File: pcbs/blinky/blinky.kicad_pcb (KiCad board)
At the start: 4 copper layers, 64 x 72 mm, 184 parts, among them J1 JACK IN, J2 NEOPIXEL, Q1 PMBT2222A,215, SW1 TACTILE, SW2 POWER, U1 ATSAMD21E17, U2 MIC5225-3.3YM5, U3 TSOP75438WTT, U4 IS31FL3731-SALS2

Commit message: Gerbers for first prototype production
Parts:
- added H5: Mouse Bites, Joels KiCad Footprint Library:Mouse_Bite_5mm_Wide, F.Cu at (163.5, 80.5)
- added H6: Mouse Bites, Joels KiCad Footprint Library:Mouse_Bite_5mm_Wide, F.Cu at (219.5, 80.5)
- added H7: JLCPCB Mounting Hole, Joels KiCad Footprint Library:JCLPCB_Tooling_Hole, F.Cu at (158.5, 45.0)
- added H8: JLCPCB Mounting Hole, Joels KiCad Footprint Library:JCLPCB_Tooling_Hole, F.Cu at (158.5, 106.5)
- added H9: JLCPCB Mounting Hole, Joels KiCad Footprint Library:JCLPCB_Tooling_Hole, F.Cu at (221.5, 106.0)
- moved H1 3.61 mm to (158.5, 40.5)
- moved H3 3.61 mm to (221.5, 40.5)
- moved FID1 2.00 mm to (158.5, 86.0)
- moved FID2 2.00 mm to (221.5, 81.0)
- moved FID3 2.00 mm to (221.5, 99.0)
- moved H2 2.00 mm to (158.5, 110.5)
- moved H4 2.00 mm to (221.5, 110.5)
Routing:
- net Net-(BT1-Pad1): track 67.6 -> 65.9 mm
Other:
- board size 64 x 72 mm -> 68 x 76 mm
- board text added: "build 002"
- board text removed: "VSCORE"
- board text removed: "build 001"

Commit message: Updated blinky schematic (ARM) for latest technology
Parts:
- removed BT1, BT2: CR2032, Joels KiCad Footprint Library:BatteryHolder_Keystone_3034_Minimum_Pad
- removed C1: 100uF 6.3V, Capacitor_SMD:C_1206_3216Metric
- removed C10, C11: 10uF, Capacitor_SMD:C_0603_1608Metric
- removed C2, C7: 1uF, Capacitor_SMD:C_0603_1608Metric
- removed C3, C4, C8, C9: 0.1uF, Capacitor_SMD:C_0603_1608Metric
- removed C5: 1.0uF, Capacitor_SMD:C_0603_1608Metric
- removed C6: 2.2uF, Capacitor_SMD:C_0603_1608Metric
- removed D1.1, D1.10, D1.11, D1.12, D1.13, D1.14, D1.15, D1.16, D1.2, D1.3, D1.4, D1.5, D1.6, D1.7, D1.8, D1.9, D2.1, D2.10, D2.11, D2.12, D2.13, D2.14, D2.15, D2.16, D2.2, D2.3, D2.4, D2.5, D2.6, D2.7, D2.8, D2.9, D3.1, D3.10, D3.11, D3.12, D3.13, D3.14, D3.15, D3.16, D3.2, D3.3, D3.4, D3.5, D3.6, D3.7, D3.8, D3.9, D4.1, D4.10, D4.11, D4.12, D4.13, D4.14, D4.15, D4.16, D4.2, D4.3, D4.4, D4.5, D4.6, D4.7, D4.8, D4.9, D5.1, D5.10, D5.11, D5.12, D5.13, D5.14, D5.15, D5.16, D5.2, D5.3, D5.4, D5.5, D5.6, D5.7, D5.8, D5.9, D6.1, D6.10, D6.11, D6.12, D6.13, D6.14, D6.15, D6.16, D6.2, D6.3, D6.4, D6.5, D6.6, D6.7, D6.8, D6.9, D7.1, D7.10, D7.11, D7.12, D7.13, D7.14, D7.15, D7.16, D7.2, D7.3, D7.4, D7.5, D7.6, D7.7, D7.8, D7.9, D8.1, D8.10, D8.11, D8.12, D8.13, D8.14, D8.15, D8.16, D8.2, D8.3, D8.4, D8.5, D8.6, D8.7, D8.8, D8.9, D9.1, D9.10, D9.11, D9.12, D9.13, D9.14, D9.15, D9.16, D9.2, D9.3, D9.4, D9.5, D9.6, D9.7, D9.8, D9.9: LED, Joels KiCad Footprint Library:LED_0603_For_Blinky
- removed D145: IR LED, LED_SMD:LED_0805_2012Metric
- removed FID1, FID2, FID3: Fiducial, Fiducial:Fiducial_1mm_Mask2mm
- removed H1, H2, H3, H4: MountingHole, MountingHole:MountingHole_2mm
- removed H5, H6: Mouse Bites, Joels KiCad Footprint Library:Mouse_Bite_5mm_Wide
- removed H7, H8, H9: JLCPCB Mounting Hole, Joels KiCad Footprint Library:JCLPCB_Tooling_Hole
- removed J1: JACK IN, Joels KiCad Footprint Library:Debug_Pad_02x05
- removed J2: NEOPIXEL, Joels KiCad Footprint Library:Debug_Pad_01x03
- removed Q1: PMBT2222A,215, Joels KiCad Footprint Library:NXP-TO-236AB-0-0-0
- removed R1: 10kΩ, Resistor_SMD:R_0603_1608Metric
- removed R10, R5, R6, R7, R8, R9: 20K, Resistor_SMD:R_0603_1608Metric
- removed R2: 330Ω, Resistor_SMD:R_0603_1608Metric
- removed R3: 47Ω, Resistor_SMD:R_0603_1608Metric
- removed R4: 470Ω, Resistor_SMD:R_0603_1608Metric
- removed SW1: TACTILE, Joels KiCad Footprint Library:TL9320AF400QG
- removed SW2: POWER, Joels KiCad Footprint Library:CK-JS102011JAQN-0-0-MFG
- removed U1: ATSAMD21E17, Joels KiCad Footprint Library:ATSAMD21E17_32Pin_TQFP
- removed U2: MIC5225-3.3YM5, Joels KiCad Footprint Library:MIC5225-SOT23-5LD
- removed U3: TSOP75438WTT, Joels KiCad Footprint Library:TSOP75438WTT
- removed U4: IS31FL3731-SALS2, Package_SO:SSOP-28_5.3x10.2mm_P0.65mm
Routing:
- net +3V3: track 156.3 -> 0.00 mm, vias 1 -> 0
- net /USB5V: track 93.9 -> 0.00 mm, vias 1 -> 0
- net /CA1: track 80.3 -> 0.00 mm, vias 2 -> 0
- net Net-(BT1-Pad2): track 79.0 -> 0.00 mm
- net /CA2: track 78.3 -> 0.00 mm, vias 4 -> 0
- net /CA5: track 78.3 -> 0.00 mm, vias 10 -> 0
- net /CA9: track 77.7 -> 0.00 mm, vias 2 -> 0
- net /CA3: track 76.9 -> 0.00 mm, vias 7 -> 0
- net /CB9: track 74.8 -> 0.00 mm, vias 2 -> 0
- net /CA4: track 74.8 -> 0.00 mm, vias 8 -> 0
- net /CA8: track 74.7 -> 0.00 mm, vias 15 -> 0
- net /CA7: track 74.1 -> 0.00 mm, vias 14 -> 0
- net /A6: track 73.4 -> 0.00 mm, vias 2 -> 0
- net /CA6: track 73.4 -> 0.00 mm, vias 13 -> 0
- net /CB8: track 73.1 -> 0.00 mm, vias 16 -> 0
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- removed copper zone on B.Cu, net GND
- removed copper zone on F.Cu, net GND
- removed copper zone on In1.Cu, net GND
- removed copper zone on In2.Cu, net GND
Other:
- board outline removed
- board text removed: "BLINKENLIGHT CONTROL"
- board text removed: "BURNING MAN 2022"
- board text removed: "COMMUNICATE"
- board text removed: "CR-2032 FLAT SIDE (+) UP"
- board text removed: "PUSHBUTTON"
- board text removed: "Power"
- board text removed: "TURTLE BRAIN"
- board text removed: "TURTLE SPACEPORT 2022"
- board text removed: "WAKING DREAMS"
- board text removed: "build 002"

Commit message: started work on the pcb
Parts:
- added BT1: CR2032, Joels KiCad Footprint Library:BatteryHolder_Keystone_3034_Minimum_Pad, B.Cu at (82.3, 116.0)
- added BT2: CR2032, Joels KiCad Footprint Library:BatteryHolder_Keystone_3034_Minimum_Pad, B.Cu at (82.3, 139.9)
- added C1: 100uF 6.3V, Capacitor_SMD:C_1206_3216Metric, F.Cu at (73.7, 165.8)
- added C10: 10uF, Capacitor_SMD:C_0603_1608Metric, F.Cu at (153.4, 114.3)
- added C11: 10uF, Capacitor_SMD:C_0603_1608Metric, F.Cu at (129.6, 137.8)
- added C2: 1uF, Capacitor_SMD:C_0603_1608Metric, F.Cu at (141.9, 133.9)
- added C3: 0.1uF, Capacitor_SMD:C_0603_1608Metric, F.Cu at (137.7, 137.0)
- added C4: 0.1uF, Capacitor_SMD:C_0603_1608Metric, F.Cu at (147.3, 128.3)
- added C5: 1.0uF, Capacitor_SMD:C_0603_1608Metric, F.Cu at (153.4, 121.9)
- added C6: 2.2uF, Capacitor_SMD:C_0603_1608Metric, F.Cu at (142.9, 130.8)
- added C7: 1uF, Capacitor_SMD:C_0603_1608Metric, F.Cu at (133.9, 134.5)
- added C8: 0.1uF, Capacitor_SMD:C_0603_1608Metric, F.Cu at (125.6, 137.8)
- added C9: 0.1uF, Capacitor_SMD:C_0603_1608Metric, F.Cu at (138.9, 128.9)
- added D145: IR LED, LED_SMD:LED_0805_2012Metric, F.Cu at (103.9, 99.0)
- added IC1: TSOP36438TT, Joels KiCad Footprint Library:TSOP36438TT, F.Cu at (106.5, 105.4)
- added J1: JACK IN, Joels KiCad Footprint Library:SOIC_clipProgSmall, F.Cu at (119.3, 137.6)
- added J3: CA1-9, Connector_PinHeader_2.54mm:PinHeader_1x09_P2.54mm_Vertical, F.Cu at (92.2, 102.7)
- added J4: CB1-9, Connector_PinHeader_2.54mm:PinHeader_1x09_P2.54mm_Vertical, F.Cu at (92.2, 153.4)
- added Q1: PMBT2222A,215, Joels KiCad Footprint Library:NXP-TO-236AB-0-0-0, F.Cu at (111.5, 99.3)
- added R1: 10kΩ, Resistor_SMD:R_0603_1608Metric, F.Cu at (143.3, 125.8)
- added R10: 20K, Resistor_SMD:R_0603_1608Metric, F.Cu at (157.5, 116.8)
- added R2: 330Ω, Resistor_SMD:R_0603_1608Metric, F.Cu at (153.4, 116.8)
- added R3: 47Ω, Resistor_SMD:R_0603_1608Metric, F.Cu at (138.9, 131.4)
- added R4: 470Ω, Resistor_SMD:R_0603_1608Metric, F.Cu at (157.5, 114.3)
- added R5: 20K, Resistor_SMD:R_0603_1608Metric, F.Cu at (143.3, 128.3)
- added R6: 20K, Resistor_SMD:R_0603_1608Metric, F.Cu at (133.7, 137.8)
- added R7: 20K, Resistor_SMD:R_0603_1608Metric, F.Cu at (137.9, 134.5)
- added R8: 20K, Resistor_SMD:R_0603_1608Metric, F.Cu at (147.3, 125.8)
- added R9: 20K, Resistor_SMD:R_0603_1608Metric, F.Cu at (153.4, 119.4)
- added S1: JS202011JCQN, Joels KiCad Footprint Library:CK-JS202011JCQN, F.Cu at (86.9, 171.9)
- added SW1: TACTILE, Joels KiCad Footprint Library:TL9320AF400QG, F.Cu at (59.5, 102.1)
- added U1: ATSAMD21E17, Joels KiCad Footprint Library:ATSAMD21E17_32Pin_TQFP, F.Cu at (60.8, 118.1)
- added U2: MIC5225-3.3YM5, Joels KiCad Footprint Library:MIC5225-SOT23-5LD, F.Cu at (87.2, 166.6)
- added U4: IS31FL3731-SALS2, Package_SO:SSOP-28_5.3x10.2mm_P0.65mm, F.Cu at (106.7, 117.6)

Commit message: routing this board here
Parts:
- added D1.1: LED, Joels KiCad Footprint Library:LED_0603_For_Blinky, F.Cu at (93.0, 107.2)
- added D1.10: LED, Joels KiCad Footprint Library:LED_0603_For_Blinky, F.Cu at (93.0, 131.2)
- added D1.11: LED, Joels KiCad Footprint Library:LED_0603_For_Blinky, F.Cu at (93.0, 133.9)
- added D1.12: LED, Joels KiCad Footprint Library:LED_0603_For_Blinky, F.Cu at (93.0, 136.6)
- added D1.13: LED, Joels KiCad Footprint Library:LED_0603_For_Blinky, F.Cu at (93.0, 139.2)
- added D1.14: LED, Joels KiCad Footprint Library:LED_0603_For_Blinky, F.Cu at (93.0, 141.9)
- added D1.15: LED, Joels KiCad Footprint Library:LED_0603_For_Blinky, F.Cu at (93.0, 144.6)
- added D1.16: LED, Joels KiCad Footprint Library:LED_0603_For_Blinky, F.Cu at (93.0, 147.2)
- added D1.2: LED, Joels KiCad Footprint Library:LED_0603_For_Blinky, F.Cu at (93.0, 109.9)
- added D1.3: LED, Joels KiCad Footprint Library:LED_0603_For_Blinky, F.Cu at (93.0, 112.6)
- added D1.4: LED, Joels KiCad Footprint Library:LED_0603_For_Blinky, F.Cu at (93.0, 115.2)
- added D1.5: LED, Joels KiCad Footprint Library:LED_0603_For_Blinky, F.Cu at (93.0, 117.9)
- added D1.6: LED, Joels KiCad Footprint Library:LED_0603_For_Blinky, F.Cu at (93.0, 120.6)
- added D1.7: LED, Joels KiCad Footprint Library:LED_0603_For_Blinky, F.Cu at (93.0, 123.2)
- added D1.8: LED, Joels KiCad Footprint Library:LED_0603_For_Blinky, F.Cu at (93.0, 125.9)
- added D1.9: LED, Joels KiCad Footprint Library:LED_0603_For_Blinky, F.Cu at (93.0, 128.6)
- added D2.1: LED, Joels KiCad Footprint Library:LED_0603_For_Blinky, F.Cu at (90.3, 107.2)
- added D2.10: LED, Joels KiCad Footprint Library:LED_0603_For_Blinky, F.Cu at (90.3, 131.2)
- added D2.11: LED, Joels KiCad Footprint Library:LED_0603_For_Blinky, F.Cu at (90.3, 133.9)
- added D2.12: LED, Joels KiCad Footprint Library:LED_0603_For_Blinky, F.Cu at (90.3, 136.6)
- added D2.13: LED, Joels KiCad Footprint Library:LED_0603_For_Blinky, F.Cu at (90.3, 139.2)
- added D2.14: LED, Joels KiCad Footprint Library:LED_0603_For_Blinky, F.Cu at (90.3, 141.9)
- added D2.15: LED, Joels KiCad Footprint Library:LED_0603_For_Blinky, F.Cu at (90.3, 144.6)
- added D2.16: LED, Joels KiCad Footprint Library:LED_0603_For_Blinky, F.Cu at (90.3, 147.2)
- added D2.2: LED, Joels KiCad Footprint Library:LED_0603_For_Blinky, F.Cu at (90.3, 109.9)
- added D2.3: LED, Joels KiCad Footprint Library:LED_0603_For_Blinky, F.Cu at (90.3, 112.6)
- added D2.4: LED, Joels KiCad Footprint Library:LED_0603_For_Blinky, F.Cu at (90.3, 115.2)
- added D2.5: LED, Joels KiCad Footprint Library:LED_0603_For_Blinky, F.Cu at (90.3, 117.9)
- added D2.6: LED, Joels KiCad Footprint Library:LED_0603_For_Blinky, F.Cu at (90.3, 120.6)
- added D2.7: LED, Joels KiCad Footprint Library:LED_0603_For_Blinky, F.Cu at (90.3, 123.2)
- added D2.8: LED, Joels KiCad Footprint Library:LED_0603_For_Blinky, F.Cu at (90.3, 125.9)
- added D2.9: LED, Joels KiCad Footprint Library:LED_0603_For_Blinky, F.Cu at (90.3, 128.6)
- added D3.1: LED, Joels KiCad Footprint Library:LED_0603_For_Blinky, F.Cu at (87.6, 107.2)
- added D3.10: LED, Joels KiCad Footprint Library:LED_0603_For_Blinky, F.Cu at (87.6, 131.2)
- added D3.11: LED, Joels KiCad Footprint Library:LED_0603_For_Blinky, F.Cu at (87.6, 133.9)
- added D3.12: LED, Joels KiCad Footprint Library:LED_0603_For_Blinky, F.Cu at (87.6, 136.6)
- added D3.13: LED, Joels KiCad Footprint Library:LED_0603_For_Blinky, F.Cu at (87.6, 139.2)
- added D3.14: LED, Joels KiCad Footprint Library:LED_0603_For_Blinky, F.Cu at (87.6, 141.9)
- added D3.15: LED, Joels KiCad Footprint Library:LED_0603_For_Blinky, F.Cu at (87.6, 144.6)
- added D3.16: LED, Joels KiCad Footprint Library:LED_0603_For_Blinky, F.Cu at (87.6, 147.2)
- added D3.2: LED, Joels KiCad Footprint Library:LED_0603_For_Blinky, F.Cu at (87.6, 109.9)
- added D3.3: LED, Joels KiCad Footprint Library:LED_0603_For_Blinky, F.Cu at (87.6, 112.6)
- added D3.4: LED, Joels KiCad Footprint Library:LED_0603_For_Blinky, F.Cu at (87.6, 115.2)
- added D3.5: LED, Joels KiCad Footprint Library:LED_0603_For_Blinky, F.Cu at (87.6, 117.9)
- added D3.6: LED, Joels KiCad Footprint Library:LED_0603_For_Blinky, F.Cu at (87.6, 120.6)
- added D3.7: LED, Joels KiCad Footprint Library:LED_0603_For_Blinky, F.Cu at (87.6, 123.2)
- added D3.8: LED, Joels KiCad Footprint Library:LED_0603_For_Blinky, F.Cu at (87.6, 125.9)
- added D3.9: LED, Joels KiCad Footprint Library:LED_0603_For_Blinky, F.Cu at (87.6, 128.6)
- added D4.1: LED, Joels KiCad Footprint Library:LED_0603_For_Blinky, F.Cu at (85.0, 107.2)
- added D4.10: LED, Joels KiCad Footprint Library:LED_0603_For_Blinky, F.Cu at (85.0, 131.2)
- added D4.11: LED, Joels KiCad Footprint Library:LED_0603_For_Blinky, F.Cu at (85.0, 133.9)
- added D4.12: LED, Joels KiCad Footprint Library:LED_0603_For_Blinky, F.Cu at (85.0, 136.6)
- added D4.13: LED, Joels KiCad Footprint Library:LED_0603_For_Blinky, F.Cu at (85.0, 139.2)
- added D4.14: LED, Joels KiCad Footprint Library:LED_0603_For_Blinky, F.Cu at (85.0, 141.9)
- added D4.15: LED, Joels KiCad Footprint Library:LED_0603_For_Blinky, F.Cu at (85.0, 144.6)
- added D4.16: LED, Joels KiCad Footprint Library:LED_0603_For_Blinky, F.Cu at (85.0, 147.2)
- added D4.2: LED, Joels KiCad Footprint Library:LED_0603_For_Blinky, F.Cu at (85.0, 109.9)
- added D4.3: LED, Joels KiCad Footprint Library:LED_0603_For_Blinky, F.Cu at (85.0, 112.6)
- added D4.4: LED, Joels KiCad Footprint Library:LED_0603_For_Blinky, F.Cu at (85.0, 115.2)
- added D4.5: LED, Joels KiCad Footprint Library:LED_0603_For_Blinky, F.Cu at (85.0, 117.9)
- added D4.6: LED, Joels KiCad Footprint Library:LED_0603_For_Blinky, F.Cu at (85.0, 120.6)
- added D4.7: LED, Joels KiCad Footprint Library:LED_0603_For_Blinky, F.Cu at (85.0, 123.2)
- added D4.8: LED, Joels KiCad Footprint Library:LED_0603_For_Blinky, F.Cu at (85.0, 125.9)
- added D4.9: LED, Joels KiCad Footprint Library:LED_0603_For_Blinky, F.Cu at (85.0, 128.6)
- added D5.1: LED, Joels KiCad Footprint Library:LED_0603_For_Blinky, F.Cu at (82.3, 107.2)
- added D5.10: LED, Joels KiCad Footprint Library:LED_0603_For_Blinky, F.Cu at (82.3, 131.2)
- added D5.11: LED, Joels KiCad Footprint Library:LED_0603_For_Blinky, F.Cu at (82.3, 133.9)
- added D5.12: LED, Joels KiCad Footprint Library:LED_0603_For_Blinky, F.Cu at (82.3, 136.6)
- added D5.13: LED, Joels KiCad Footprint Library:LED_0603_For_Blinky, F.Cu at (82.3, 139.2)
- added D5.14: LED, Joels KiCad Footprint Library:LED_0603_For_Blinky, F.Cu at (82.3, 141.9)
- added D5.15: LED, Joels KiCad Footprint Library:LED_0603_For_Blinky, F.Cu at (82.3, 144.6)
- added D5.16: LED, Joels KiCad Footprint Library:LED_0603_For_Blinky, F.Cu at (82.3, 147.2)
- added D5.2: LED, Joels KiCad Footprint Library:LED_0603_For_Blinky, F.Cu at (82.3, 109.9)
- added D5.3: LED, Joels KiCad Footprint Library:LED_0603_For_Blinky, F.Cu at (82.3, 112.6)
- added D5.4: LED, Joels KiCad Footprint Library:LED_0603_For_Blinky, F.Cu at (82.3, 115.2)
- added D5.5: LED, Joels KiCad Footprint Library:LED_0603_For_Blinky, F.Cu at (82.3, 117.9)
- added D5.6: LED, Joels KiCad Footprint Library:LED_0603_For_Blinky, F.Cu at (82.3, 120.6)
- added D5.7: LED, Joels KiCad Footprint Library:LED_0603_For_Blinky, F.Cu at (82.3, 123.2)
- added D5.8: LED, Joels KiCad Footprint Library:LED_0603_For_Blinky, F.Cu at (82.3, 125.9)
- added D5.9: LED, Joels KiCad Footprint Library:LED_0603_For_Blinky, F.Cu at (82.3, 128.6)
- added D6.1: LED, Joels KiCad Footprint Library:LED_0603_For_Blinky, F.Cu at (79.6, 107.2)
- added D6.10: LED, Joels KiCad Footprint Library:LED_0603_For_Blinky, F.Cu at (79.6, 131.2)
- added D6.11: LED, Joels KiCad Footprint Library:LED_0603_For_Blinky, F.Cu at (79.6, 133.9)
- added D6.12: LED, Joels KiCad Footprint Library:LED_0603_For_Blinky, F.Cu at (79.6, 136.6)
- added D6.13: LED, Joels KiCad Footprint Library:LED_0603_For_Blinky, F.Cu at (79.6, 139.2)
- added D6.14: LED, Joels KiCad Footprint Library:LED_0603_For_Blinky, F.Cu at (79.6, 141.9)
- added D6.15: LED, Joels KiCad Footprint Library:LED_0603_For_Blinky, F.Cu at (79.6, 144.6)
- added D6.16: LED, Joels KiCad Footprint Library:LED_0603_For_Blinky, F.Cu at (79.6, 147.2)
- added D6.2: LED, Joels KiCad Footprint Library:LED_0603_For_Blinky, F.Cu at (79.6, 109.9)
- added D6.3: LED, Joels KiCad Footprint Library:LED_0603_For_Blinky, F.Cu at (79.6, 112.6)
- added D6.4: LED, Joels KiCad Footprint Library:LED_0603_For_Blinky, F.Cu at (79.6, 115.2)
- added D6.5: LED, Joels KiCad Footprint Library:LED_0603_For_Blinky, F.Cu at (79.6, 117.9)
- added D6.6: LED, Joels KiCad Footprint Library:LED_0603_For_Blinky, F.Cu at (79.6, 120.6)
- added D6.7: LED, Joels KiCad Footprint Library:LED_0603_For_Blinky, F.Cu at (79.6, 123.2)
- added D6.8: LED, Joels KiCad Footprint Library:LED_0603_For_Blinky, F.Cu at (79.6, 125.9)
- added D6.9: LED, Joels KiCad Footprint Library:LED_0603_For_Blinky, F.Cu at (79.6, 128.6)
- added D7.1: LED, Joels KiCad Footprint Library:LED_0603_For_Blinky, F.Cu at (77.0, 107.2)
- added D7.10: LED, Joels KiCad Footprint Library:LED_0603_For_Blinky, F.Cu at (77.0, 131.2)
- added D7.11: LED, Joels KiCad Footprint Library:LED_0603_For_Blinky, F.Cu at (77.0, 133.9)
- added D7.12: LED, Joels KiCad Footprint Library:LED_0603_For_Blinky, F.Cu at (77.0, 136.6)
- added D7.13: LED, Joels KiCad Footprint Library:LED_0603_For_Blinky, F.Cu at (77.0, 139.2)
- added D7.14: LED, Joels KiCad Footprint Library:LED_0603_For_Blinky, F.Cu at (77.0, 141.9)
- added D7.15: LED, Joels KiCad Footprint Library:LED_0603_For_Blinky, F.Cu at (77.0, 144.6)
- added D7.16: LED, Joels KiCad Footprint Library:LED_0603_For_Blinky, F.Cu at (77.0, 147.2)
- added D7.2: LED, Joels KiCad Footprint Library:LED_0603_For_Blinky, F.Cu at (77.0, 109.9)
- added D7.3: LED, Joels KiCad Footprint Library:LED_0603_For_Blinky, F.Cu at (77.0, 112.6)
- added D7.4: LED, Joels KiCad Footprint Library:LED_0603_For_Blinky, F.Cu at (77.0, 115.2)
- added D7.5: LED, Joels KiCad Footprint Library:LED_0603_For_Blinky, F.Cu at (77.0, 117.9)
- added D7.6: LED, Joels KiCad Footprint Library:LED_0603_For_Blinky, F.Cu at (77.0, 120.6)
- added D7.7: LED, Joels KiCad Footprint Library:LED_0603_For_Blinky, F.Cu at (77.0, 123.2)
- added D7.8: LED, Joels KiCad Footprint Library:LED_0603_For_Blinky, F.Cu at (77.0, 125.9)
- added D7.9: LED, Joels KiCad Footprint Library:LED_0603_For_Blinky, F.Cu at (77.0, 128.6)
- added D8.1: LED, Joels KiCad Footprint Library:LED_0603_For_Blinky, F.Cu at (74.3, 107.2)
- added D8.10: LED, Joels KiCad Footprint Library:LED_0603_For_Blinky, F.Cu at (74.3, 131.2)
- added D8.11: LED, Joels KiCad Footprint Library:LED_0603_For_Blinky, F.Cu at (74.3, 133.9)
- added D8.12: LED, Joels KiCad Footprint Library:LED_0603_For_Blinky, F.Cu at (74.3, 136.6)
- added D8.13: LED, Joels KiCad Footprint Library:LED_0603_For_Blinky, F.Cu at (74.3, 139.2)
- added D8.14: LED, Joels KiCad Footprint Library:LED_0603_For_Blinky, F.Cu at (74.3, 141.9)
- added D8.15: LED, Joels KiCad Footprint Library:LED_0603_For_Blinky, F.Cu at (74.3, 144.6)
- added D8.16: LED, Joels KiCad Footprint Library:LED_0603_For_Blinky, F.Cu at (74.3, 147.2)
- added D8.2: LED, Joels KiCad Footprint Library:LED_0603_For_Blinky, F.Cu at (74.3, 109.9)
- added D8.3: LED, Joels KiCad Footprint Library:LED_0603_For_Blinky, F.Cu at (74.3, 112.6)
- added D8.4: LED, Joels KiCad Footprint Library:LED_0603_For_Blinky, F.Cu at (74.3, 115.2)
- added D8.5: LED, Joels KiCad Footprint Library:LED_0603_For_Blinky, F.Cu at (74.3, 117.9)
- added D8.6: LED, Joels KiCad Footprint Library:LED_0603_For_Blinky, F.Cu at (74.3, 120.6)
- added D8.7: LED, Joels KiCad Footprint Library:LED_0603_For_Blinky, F.Cu at (74.3, 123.2)
- added D8.8: LED, Joels KiCad Footprint Library:LED_0603_For_Blinky, F.Cu at (74.3, 125.9)
- added D8.9: LED, Joels KiCad Footprint Library:LED_0603_For_Blinky, F.Cu at (74.3, 128.6)
- added D9.1: LED, Joels KiCad Footprint Library:LED_0603_For_Blinky, F.Cu at (71.6, 107.2)
- added D9.10: LED, Joels KiCad Footprint Library:LED_0603_For_Blinky, F.Cu at (71.6, 131.2)
- added D9.11: LED, Joels KiCad Footprint Library:LED_0603_For_Blinky, F.Cu at (71.6, 133.9)
- added D9.12: LED, Joels KiCad Footprint Library:LED_0603_For_Blinky, F.Cu at (71.6, 136.6)
- added D9.13: LED, Joels KiCad Footprint Library:LED_0603_For_Blinky, F.Cu at (71.6, 139.2)
- added D9.14: LED, Joels KiCad Footprint Library:LED_0603_For_Blinky, F.Cu at (71.6, 141.9)
- added D9.15: LED, Joels KiCad Footprint Library:LED_0603_For_Blinky, F.Cu at (71.6, 144.6)
- added D9.16: LED, Joels KiCad Footprint Library:LED_0603_For_Blinky, F.Cu at (71.6, 147.2)
- added D9.2: LED, Joels KiCad Footprint Library:LED_0603_For_Blinky, F.Cu at (71.6, 109.9)
- added D9.3: LED, Joels KiCad Footprint Library:LED_0603_For_Blinky, F.Cu at (71.6, 112.6)
- added D9.4: LED, Joels KiCad Footprint Library:LED_0603_For_Blinky, F.Cu at (71.6, 115.2)
- added D9.5: LED, Joels KiCad Footprint Library:LED_0603_For_Blinky, F.Cu at (71.6, 117.9)
- added D9.6: LED, Joels KiCad Footprint Library:LED_0603_For_Blinky, F.Cu at (71.6, 120.6)
- added D9.7: LED, Joels KiCad Footprint Library:LED_0603_For_Blinky, F.Cu at (71.6, 123.2)
- added D9.8: LED, Joels KiCad Footprint Library:LED_0603_For_Blinky, F.Cu at (71.6, 125.9)
- added D9.9: LED, Joels KiCad Footprint Library:LED_0603_For_Blinky, F.Cu at (71.6, 128.6)
- moved BT1 90.8 mm to (129.3, 38.3)
- moved BT2 89.1 mm to (129.3, 64.2)
- moved C5 63.2 mm to (109.8, 167.7)
- moved R4 63.2 mm to (113.9, 160.1)
- moved R2 63.2 mm to (109.8, 162.6)
- moved R10 57.2 mm to (103.3, 135.3), turned to 90 degrees
- moved R9 54.4 mm to (101.5, 135.3), turned to 270 degrees
- moved C10 52.1 mm to (103.3, 128.3), turned to 270 degrees
- moved R8 48.6 mm to (99.7, 135.3), turned to 270 degrees
- moved R5 48.1 mm to (96.3, 118.5), turned to 180 degrees
- moved R6 42.9 mm to (96.3, 116.7)
- moved C4 41.2 mm to (123.5, 161.9)
- moved R3 41.2 mm to (115.1, 165.0)
- moved C2 41.2 mm to (118.1, 167.5)
- moved C6 41.2 mm to (119.1, 164.4)
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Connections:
- net Net-(C8-Pad1) renamed /CFILT
- net Net-(R10-Pad1) renamed /AD
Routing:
- net /CB8: track 0.00 -> 119.0 mm, vias 0 -> 7
- net /CB9: track 0.00 -> 116.3 mm
- net /CB7: track 0.00 -> 116.2 mm, vias 0 -> 7
- net /CB6: track 0.00 -> 113.5 mm, vias 0 -> 7
- net /CB5: track 0.00 -> 110.9 mm, vias 0 -> 7
- net /CB4: track 0.00 -> 108.3 mm, vias 0 -> 7
- net /CB3: track 0.00 -> 105.7 mm, vias 0 -> 7
- net /CA8: track 0.00 -> 103.1 mm, vias 0 -> 8
- net /CB2: track 0.00 -> 103.0 mm, vias 0 -> 7
- net /CB1: track 0.00 -> 102.2 mm, vias 0 -> 8
- net /CA7: track 0.00 -> 100.8 mm, vias 0 -> 8
- net /CA6: track 0.00 -> 98.4 mm, vias 0 -> 8
- net /CA5: track 0.00 -> 96.0 mm, vias 0 -> 8
- net /CA4: track 0.00 -> 93.6 mm, vias 0 -> 8
- net /CA9: track 0.00 -> 93.5 mm, vias 0 -> 1
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- added copper zone on B.Cu, net +3V3
- added copper zone on In2.Cu, net GND
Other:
- board outline added: 135 x 97 mm
- board text added: "LEDTRIX 2.0"

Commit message: making good progress on the circuit board
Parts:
- moved C3 90.8 mm to (65.7, 128.3), turned to 270 degrees
- moved J1 87.7 mm to (45.5, 142.9)
- moved C7 77.2 mm to (101.1, 99.7), turned to 90 degrees
- moved BT1 74.0 mm to (127.1, 112.3)
- moved BT2 74.0 mm to (127.1, 138.2)
- moved C4 70.4 mm to (61.7, 128.3), turned to 270 degrees
- moved R1 67.5 mm to (59.7, 128.3), turned to 90 degrees
- moved C6 67.4 mm to (58.1, 135.7), turned to 90 degrees
- moved R3 67.2 mm to (98.9, 99.7), turned to 270 degrees
- moved C2 67.1 mm to (63.7, 128.3), turned to 270 degrees
- moved R2 62.5 mm to (57.7, 128.3), turned to 90 degrees
- moved R4 61.3 mm to (103.3, 99.7), turned to 90 degrees
- moved C5 54.5 mm to (65.7, 135.7), turned to 90 degrees
- moved D145 48.8 mm to (102.3, 141.7), turned to 180 degrees
- moved U2 40.1 mm to (61.9, 135.5), turned to 180 degrees
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- renumbered S1 to SW2, IC1 to U3
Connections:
- net Net-(C2-Pad1) renamed /VDDCORE
- net Net-(C4-Pad1) renamed /2RST
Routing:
- net /SCL: track 26.5 -> 125.2 mm, vias 0 -> 2
- net /SDA: track 23.2 -> 120.1 mm
- net /A1: track 0.00 -> 70.7 mm
- net /A2: track 0.00 -> 62.5 mm
- net /A3: track 0.00 -> 58.8 mm
- net Net-(D145-Pad1): track 0.00 -> 45.5 mm
- net GND: track 27.4 -> 53.2 mm, vias 3 -> 12
- net +3V3: track 27.6 -> 52.9 mm, vias 2 -> 7
- net +5V: track 0.00 -> 16.4 mm
- net /2RST: track 0.00 -> 13.0 mm
- net /VDDCORE: track 0.00 -> 12.2 mm
- net Net-(C7-Pad1): track 0.00 -> 10.6 mm
- net /A0: track 0.00 -> 6.23 mm
- net Net-(Q1-Pad1): track 0.00 -> 2.54 mm
- net VBUS: track 0.00 -> 2.40 mm
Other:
- outline, holes or cut-outs redrawn

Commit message: Everything is done except artistic stuff
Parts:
- moved BT1 57.2 mm to (76.9, 139.7)
- moved BT2 44.8 mm to (87.4, 117.7), turned to 270 degrees
- moved C1 26.4 mm to (65.7, 142.5), turned to 270 degrees
- moved SW2 2.23 mm to (82.3, 166.7)
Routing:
- net VBUS: track 2.40 -> 82.3 mm, vias 0 -> 3
- net /A6: track 12.8 -> 90.5 mm, vias 0 -> 2
- net Net-(BT1-Pad2): track 0.00 -> 65.9 mm
- net GND: track 53.2 -> 105.2 mm, vias 12 -> 14
- net +5V: track 16.4 -> 54.7 mm, vias 0 -> 3
- net /A3: track 58.8 -> 58.2 mm
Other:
- board text added: "CR2032 BATTERY FLAT SIDE UP"
- board text added: "ON"
- board text removed: "LEDTRIX 2.0"

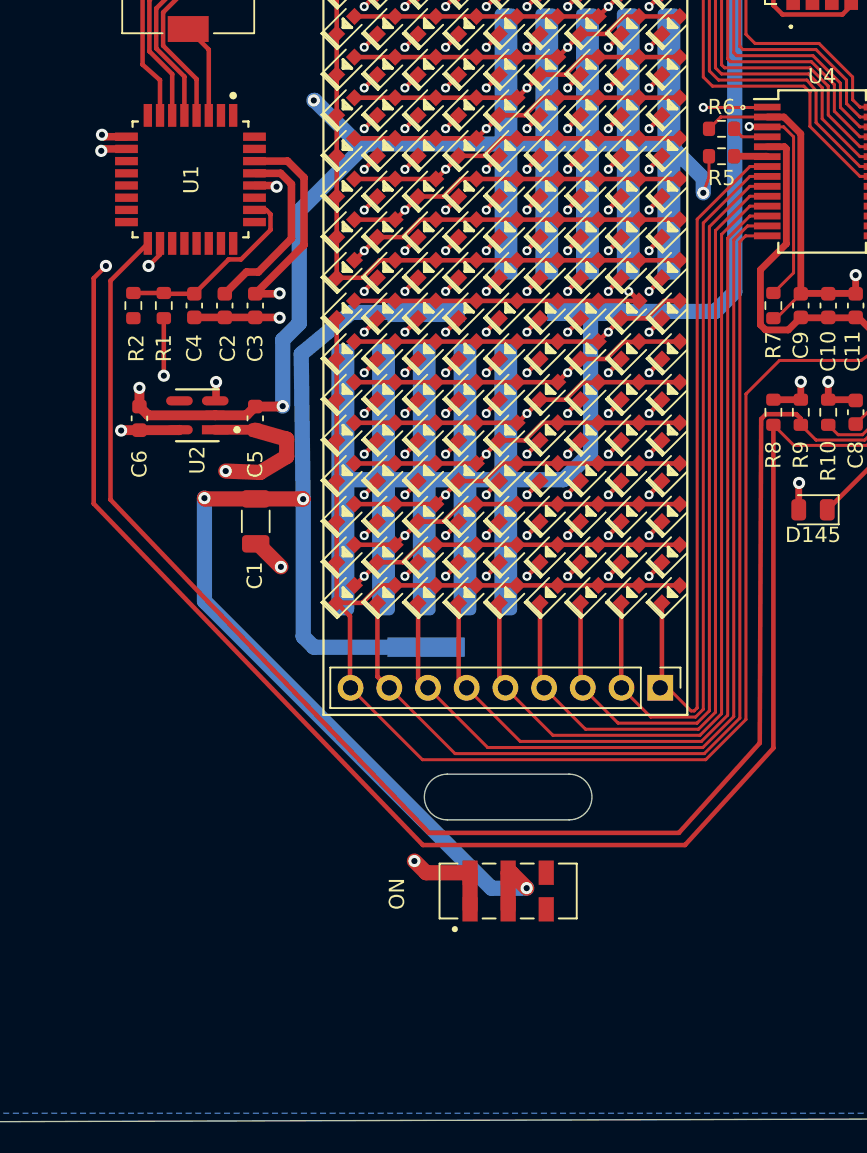
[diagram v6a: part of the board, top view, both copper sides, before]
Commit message: Moved power switch up to make board shorter
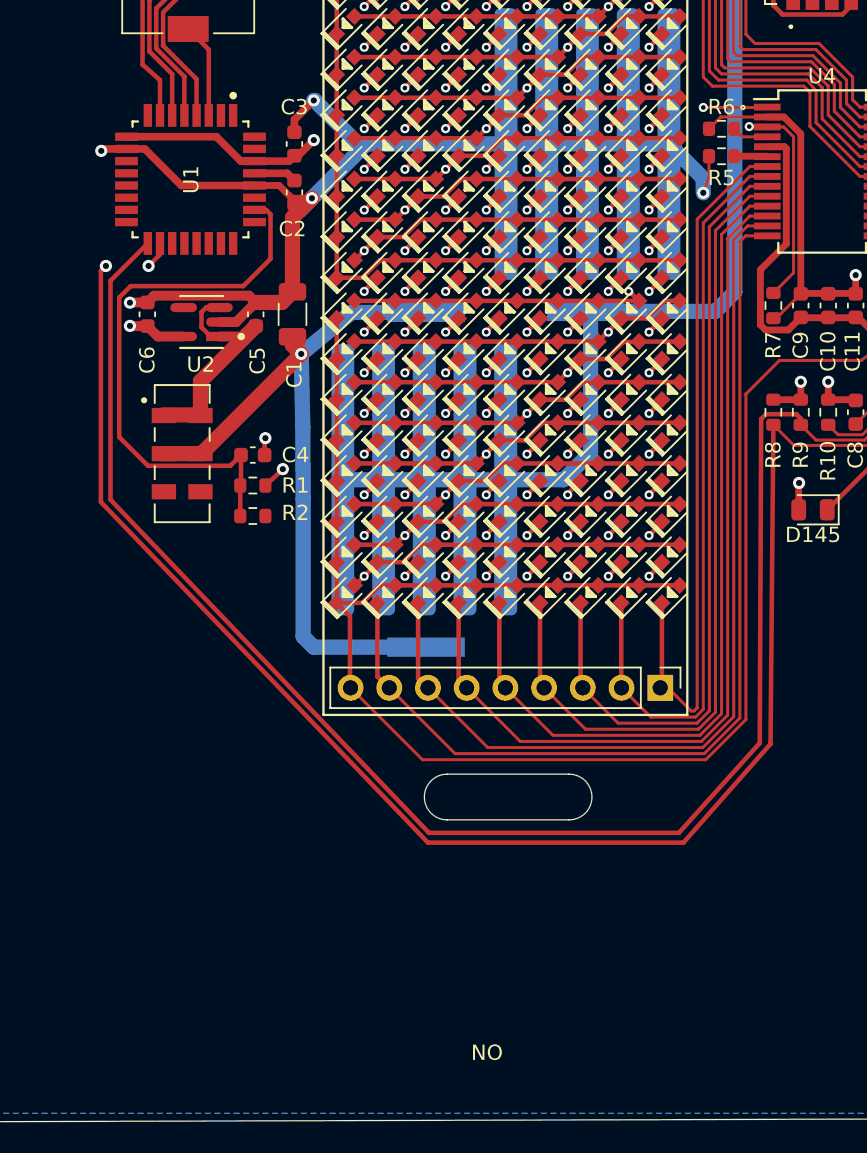
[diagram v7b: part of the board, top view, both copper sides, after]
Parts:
- moved SW2 35.8 mm to (60.9, 138.0), turned to 0 degrees
- moved R2 15.9 mm to (65.5, 142.1), turned to 180 degrees
- moved C1 13.8 mm to (68.1, 128.9), turned to 90 degrees
- moved R1 13.2 mm to (65.5, 140.1), turned to 180 degrees
- moved C3 10.9 mm to (68.2, 117.7), turned to 90 degrees
- moved C4 10.5 mm to (65.5, 138.1), turned to 0 degrees
- moved C2 8.72 mm to (68.2, 120.9)
- moved C6 6.85 mm to (58.6, 128.9)
- moved C5 6.83 mm to (65.7, 128.9)
- moved U2 6.13 mm to (62.1, 129.4)
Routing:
- net +5V: track 54.7 -> 16.2 mm, vias 3 -> 0
- net VBUS: track 82.3 -> 49.2 mm, vias 3 -> 1
- net /2RST: track 13.0 -> 37.3 mm
- net /VDDCORE: track 12.2 -> 2.82 mm
- net GND: track 105.2 -> 110.9 mm, vias 14 -> 12
- net +3V3: track 52.9 -> 48.2 mm, vias 7 -> 6
- net /SCL: track 125.2 -> 124.1 mm
